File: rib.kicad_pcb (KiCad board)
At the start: 2 copper layers, 140 x 90 mm, 92 parts, among them J1 RJ45_LED, J10 Conn_01x04_Male, J11 Screw_Terminal_01x02, J12 Screw_Terminal_01x02, J13 Screw_Terminal_01x02, J14 Conn_01x02_Male, J15 Conn_01x02_Male, J16 Conn_01x06_Male, J2 RJ45_LED, J3 RJ45_LED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

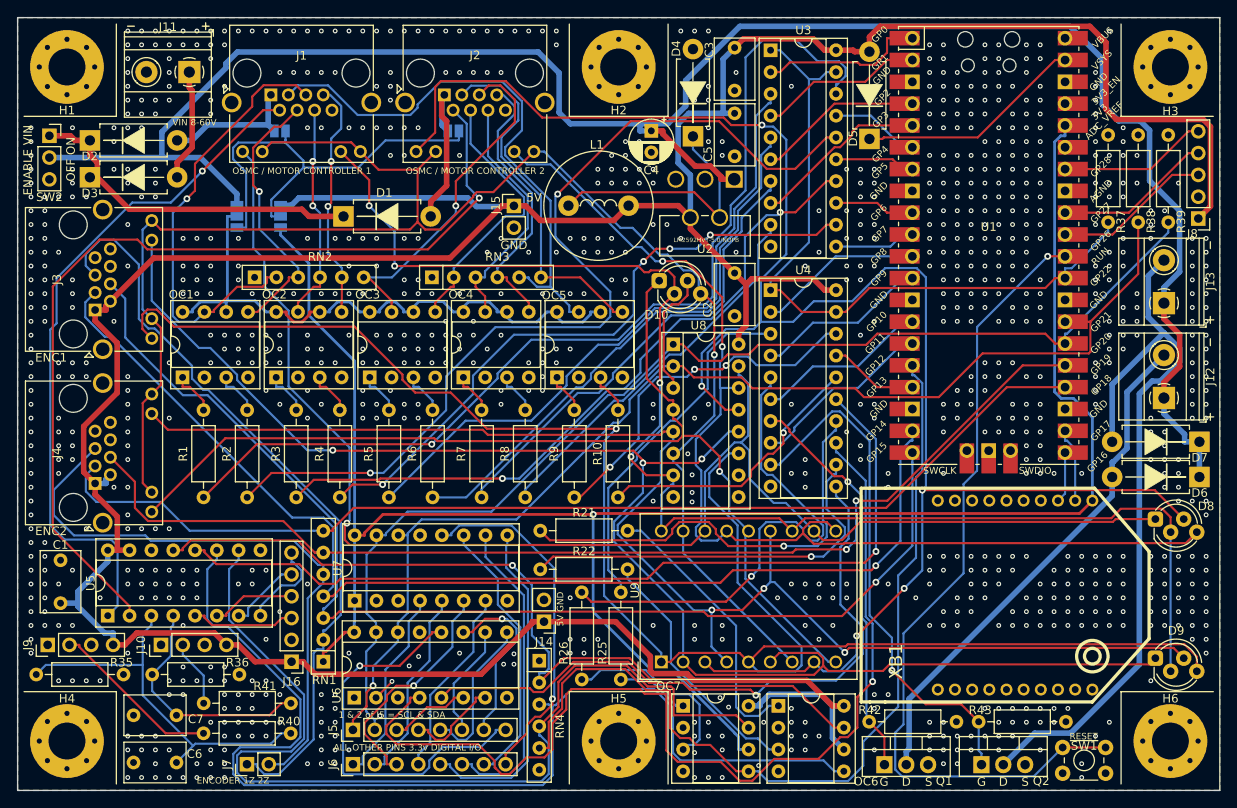
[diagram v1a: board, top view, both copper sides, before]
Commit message: Fix issues with RC1 - LED orientation, pullups, 3v3 source
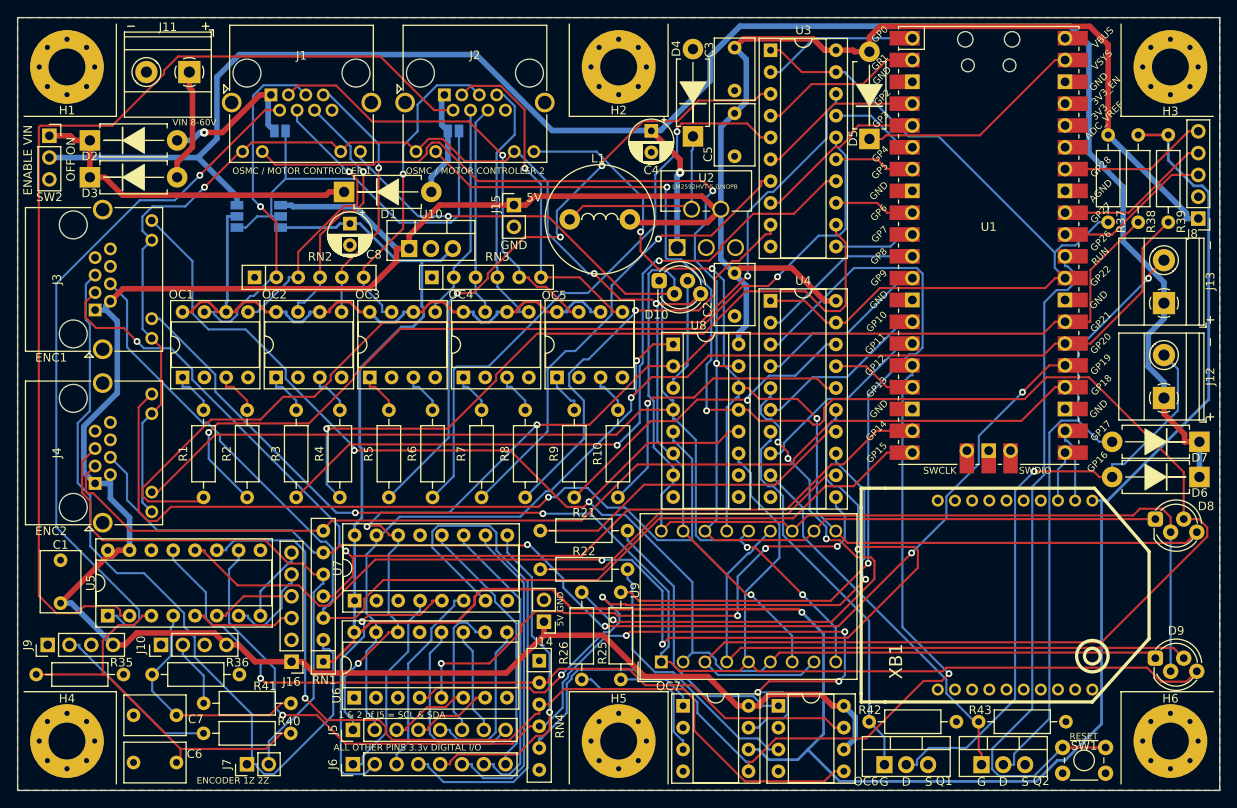
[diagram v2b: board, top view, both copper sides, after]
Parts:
- added C8: 33uF, Capacitor_THT:CP_Radial_D5.0mm_P2.50mm, F.Cu at (74.2, 71.0)
- added U10: LM3940IT-3.3, Package_TO_SOT_THT:TO-220-3_Vertical, F.Cu at (81.1, 73.9)
- RN1: value R_Network06 -> 10k_Network06
- RN2, RN3, RN4: value R_Network05 -> 2k_Network05
- moved U2 19.7 mm to (119.1, 60.6), turned to 0 degrees
- moved D1 2.85 mm to (73.5, 67.3)
- moved L1 1.61 mm to (99.8, 70.5)
- moved U4 1.24 mm to (123.2, 80.0)
- moved J15 0.10 mm to (93.3, 68.8)
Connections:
- net Net-(D6-A) renamed MOSFET1
- net Net-(D7-A) renamed MOSFET2
- J1 pad 10: CATHODE3 -> LED2
- J1 pad 11: LED1 -> CATHODE3
- J1 pad 12: CATHODE3 -> LED1
- J1 pad 9: LED2 -> CATHODE3
- J2 pad 10: CATHODE3 -> LED4
- J2 pad 11: LED3 -> CATHODE3
- J2 pad 12: CATHODE3 -> LED3
- J2 pad 9: LED4 -> CATHODE3
- J3 pad 10: CATHODE3 -> LED6
- J3 pad 11: LED5 -> CATHODE3
- J3 pad 12: CATHODE3 -> LED5
- J3 pad 9: LED6 -> CATHODE3
- J4 pad 10: CATHODE3 -> LED8
- J4 pad 11: LED7 -> CATHODE3
- J4 pad 12: CATHODE3 -> LED7
- J4 pad 9: LED8 -> CATHODE3
- R37 pad 1: GND -> 5V
- R38 pad 2: GND -> 3.3V
- R39 pad 2: GND -> 3.3V
- U1 pad 36: 3.3V -> unconnected-(U1-3V3-Pad36)
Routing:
- net 3.3V: track 228.3 -> 277.5 mm
- net Net-(U4-2Y0): track 41.9 -> 89.7 mm, vias 0 -> 1
- net Net-(J6-Pin_4): track 22.3 -> 62.0 mm
- net Net-(U4-2A2): track 117.2 -> 79.9 mm, vias 1 -> 3
- net Net-(U4-2A1): track 102.3 -> 128.6 mm, vias 1 -> 3
- net Net-(RN4-R2): track 128.3 -> 103.8 mm, vias 0 -> 1
- net Net-(J5-Pin_8): track 46.3 -> 22.3 mm, vias 1 -> 0
- net LED6: track 199.7 -> 176.4 mm, vias 1 -> 2
- net CATHODE3: track 191.9 -> 170.0 mm, vias 1 -> 4
- net 5V: track 407.4 -> 389.8 mm
- net Net-(Q2-G): track 61.1 -> 44.1 mm, vias 1 -> 0
- net LED2: track 171.7 -> 155.6 mm, vias 1 -> 2
- net Net-(U1-RUN): track 95.4 -> 80.0 mm, vias 1 -> 0
- net MOSFET2: track 87.7 -> 73.4 mm, vias 0 -> 1
- net Net-(U5-CH1): track 108.4 -> 121.6 mm, vias 1 -> 0
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
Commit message: Reroute with better trace thickness
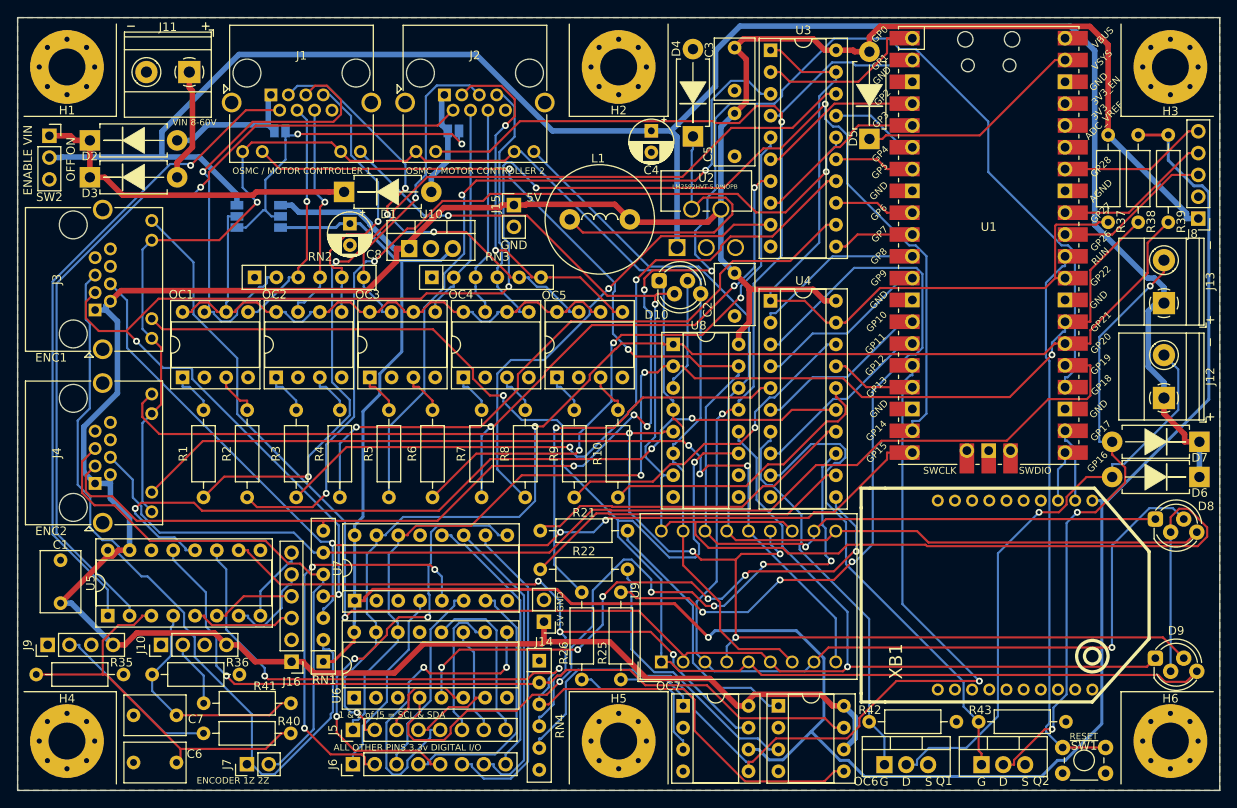
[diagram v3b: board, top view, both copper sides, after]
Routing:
- net Net-(RN1-R3): track 125.8 -> 202.4 mm, vias 2 -> 5
- net Net-(RN1-R6): track 126.6 -> 198.8 mm, vias 0 -> 5
- net Net-(RN4-R3): track 123.3 -> 84.1 mm, vias 5 -> 3
- net Net-(J6-Pin_4): track 62.0 -> 30.7 mm
- net Net-(U4-2A1): track 128.6 -> 97.4 mm
- net LED4: track 210.3 -> 183.9 mm, vias 2 -> 3
- net Net-(U5-CH1): track 121.6 -> 97.2 mm, vias 0 -> 1
- net Net-(U4-2Y1): track 68.2 -> 47.6 mm, vias 4 -> 1
- net Net-(J5-Pin_5): track 19.7 -> 37.6 mm, vias 0 -> 2
- net LED1: track 160.8 -> 177.2 mm, vias 1 -> 2
- net Net-(U1-RUN): track 80.0 -> 64.5 mm
- net LED5: track 172.1 -> 187.6 mm
- net LED3: track 130.8 -> 115.7 mm, vias 3 -> 0
- net Net-(J6-Pin_5): track 39.2 -> 54.0 mm, vias 1 -> 3
- net Net-(J6-Pin_2): track 33.6 -> 48.1 mm, vias 1 -> 3
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
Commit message: Fix track hole clearance. crashes when trying to do via stitching
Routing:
- net Net-(J7-Pin_2): track 63.3 -> 69.5 mm
- net Net-(J7-Pin_1): track 90.7 -> 91.6 mm

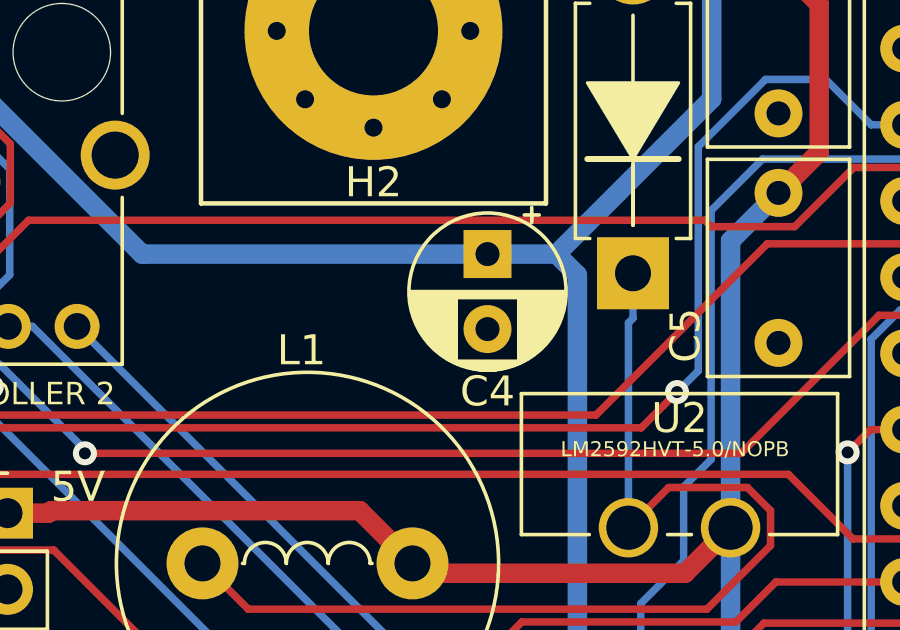
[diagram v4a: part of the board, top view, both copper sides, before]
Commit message: Make space for heatsinks
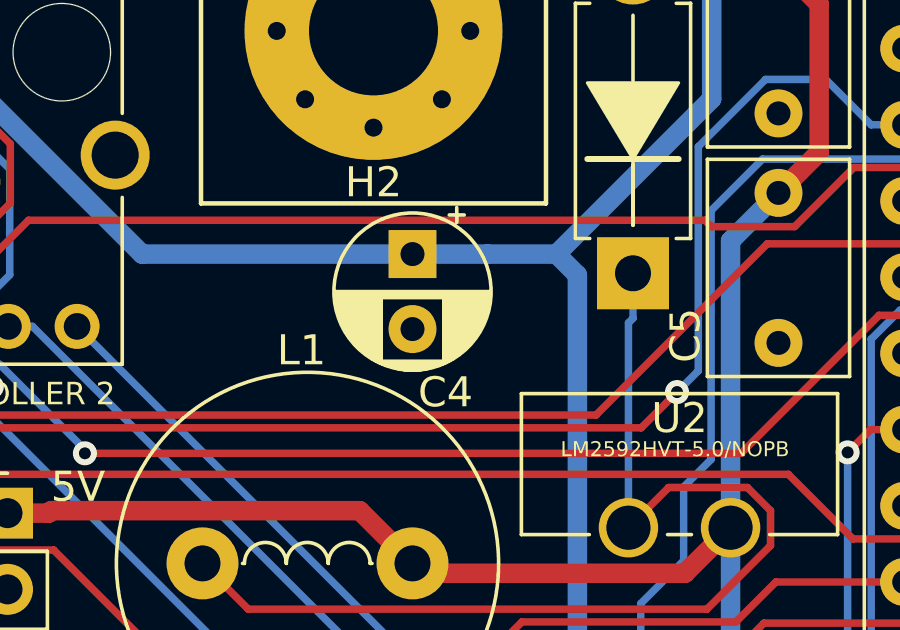
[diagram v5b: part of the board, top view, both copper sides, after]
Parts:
- moved C4 2.50 mm to (106.8, 60.2)
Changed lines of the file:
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@@
   )
   (footprint "Capacitor_THT:CP_Radial_D5.0mm_P2.50mm" (layer "F.Cu")
-    (at 109.3 60.1898 -90)
+    (at 106.8 60.1898 -90)
     (descr "CP, Radial series, Radial, pin pitch=2.50mm, , diameter=5mm, Electrolytic Capacitor")
     (tags "CP Radial series Radial pin pitch 2.50mm  diameter 5mm Electrolytic Capacitor")
@@
     (property "ki_keywords" "cap capacitor")
     (attr through_hole)
-    (fp_text reference "C4" (at 4.580672 0) (layer "F.SilkS")
+    (fp_text reference "C4" (at 4.6102 -1.1) (layer "F.SilkS")
         (effects (font (size 1 1) (thickness 0.15)))
     )
